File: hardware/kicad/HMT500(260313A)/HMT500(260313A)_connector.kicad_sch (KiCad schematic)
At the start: 10 parts, among them J1 SM08B-GHS-TB, J5 CHASSIS wire

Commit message: Schematic v0.9 + placement rev 4: apply triple-review A/B items, re-review fixes
- Power: OVP 32.6 V (R5 36.5k), D2 TVS3301, C2 2.2u 100V, buck input 220n x2,
  U2 pin 3 = SW; TPS26611 +Vs emitter-follower clamp (Q1 MMBTA06, R50, D50 27V)
- RS-485: THVD2410, DE 10k pull-down (R60) for in-house bootloader
- MCU: SGOOD on PA0/PA4, CS_CDC PA15, VIN_SENSE PB0, LATCH/CS pull-ups,
  SWD no-connect removed, netlist checker flags no-connect on used pins
- Analog: OPA197 V+ = DAC AVDD, R31/R41 100k, local caps; X7R throughout
- New aux sheet; SOT-23 and R1206 footprints; parts list and JLC files
- Placement: pin-targeted hints, MCU decaps under U4, chassis parts grouped
  in front, J5 keep-out 3.3 mm, CHASSIS netclass; 102/102 parts placed
- Docs: final review H table, decision #32, circuit design, placement rev 4

Co-Authored-By: Claude Opus 5.5 <noreply@anthropic.com>
Claude-Session: https://claude.ai/code/session_01JA2o8uJsqp9Vzsg4b665ev
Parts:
- D2: value SMBJ33CA -> TVS3301DRBR; footprint Diode_SMD:D_SMB -> HMT500_260313A:Texas_DRB0008A_PadFloat; symbol HMT500_260313A:TVS_BI -> HMT500_260313A:TVS3301
- R2: value 1M -> 1M HV; footprint Resistor_SMD:R_0603_1608Metric -> Resistor_SMD:R_1206_3216Metric
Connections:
- net GND: now also D2.5, D2.6, D2.7, D2.8; no longer D2.2
- net VIN_F: now also D2.2, D2.3, D2.4
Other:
- note added: "4.7n Y2 / 1M HV"
- note added: "SMDJ 3 kW (1st) -> R1 -> TVS3301 flat clamp (2nd) -> eFuse on sheet Power"
- note added: "TI 평탄 클램프 ±33 V, 42.5 V @ 27 A — 음(-) 서지에서 eFuse IN–OUT을 -70 V/10 ms 이내로 (전원 ≤ 28 V, 여유 작음 → 몰딩 전 서지 시험). DC 입력 33 V 초과 금지 (v0.9, 이전 SMBJ33CA)"
- note added: "TVS3301DRBR"
- note added: "Y2 안전 콘덴서 + 1 MΩ 고전압 칩 저항 1206 (사용 전압 ≥ 1 kV — GDT 방전 전 임펄스를 견딤, 몰딩 안)"
- note removed: "4.7n Y2 / 1M"
- note removed: "SMBJ33CA"
- note removed: "SMDJ 3 kW (1st) -> R1 -> SMBJ (2nd) -> eFuse on sheet Power"
- note removed: "TVS 양방향 600 W, 33 V — eFuse 정격 이하로 제한"
- note removed: "Y2 안전 콘덴서 + 1 MΩ 정전기 방전 경로"

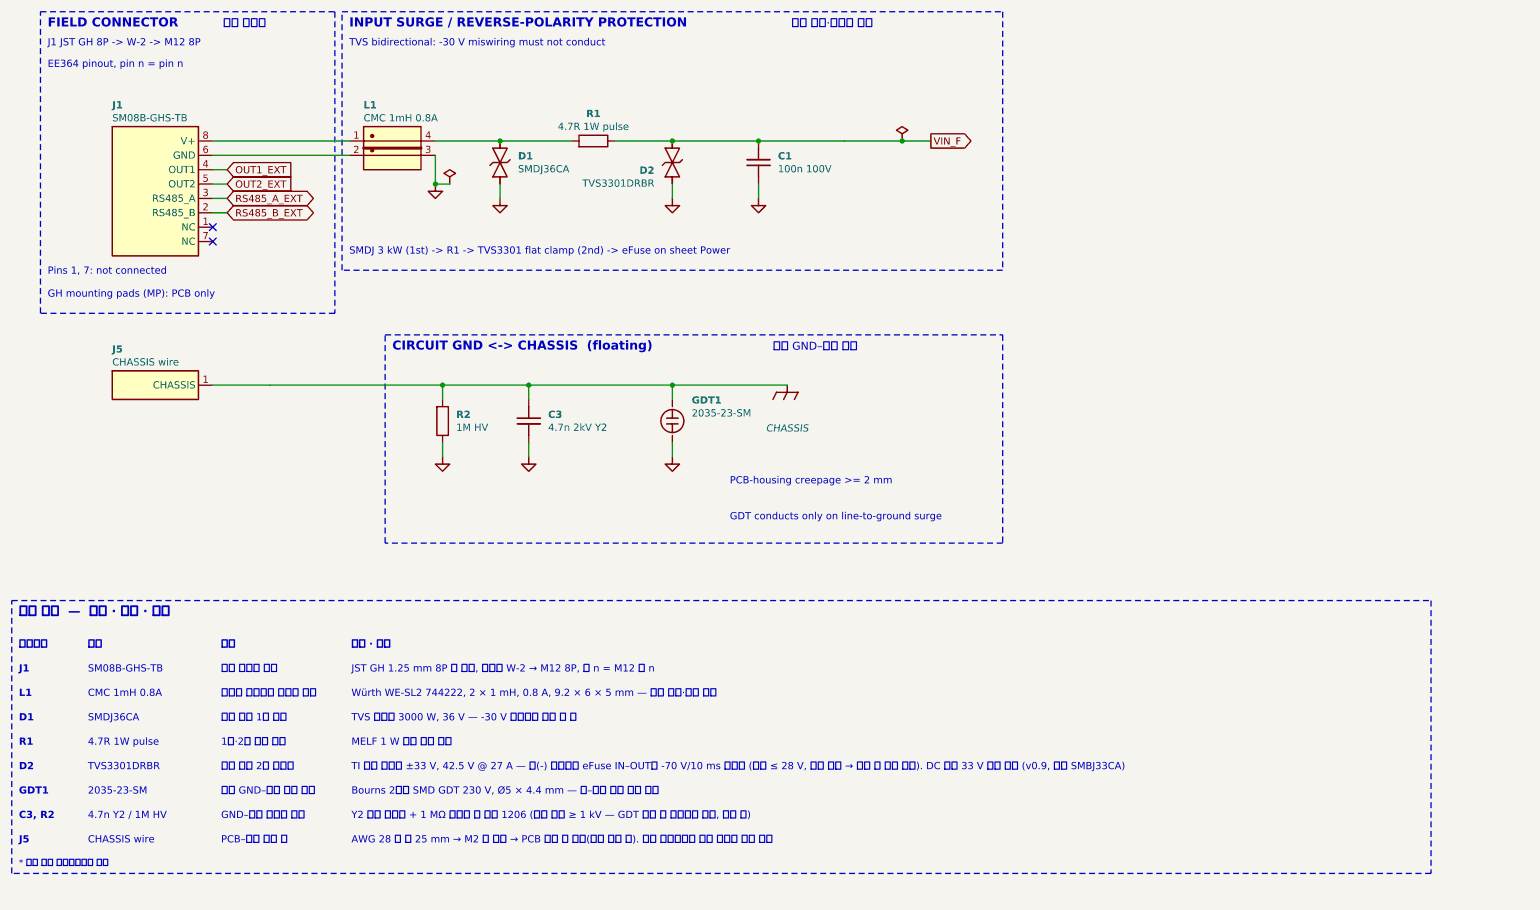
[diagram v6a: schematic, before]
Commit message: Map BOM to JLCPCB/LCSC parts (decision #34) and re-place
- 50 of 55 BOM lines have LCSC numbers (make_parts_list.LCSC); parts list
  gets LCSC / JLC class columns; JLC BOM and harness order filled
- Keep MCU (125 C grade), LMR36006, R19 precision ref and pulse resistors
  via JLC global sourcing
- LCSC-driven footprint changes: C6/C10 1210, C16/C17 0805, R1 2512,
  L2 XAL4040; C3 2 kV X7R 1812, GDT 2035-25, L1 SRF0905 (to verify)
- Re-placed: 102/102, netlist 77/77, assembly sim 23 OK

Co-Authored-By: Claude Opus 5.5 <noreply@anthropic.com>
Claude-Session: https://claude.ai/code/session_01JA2o8uJsqp9Vzsg4b665ev
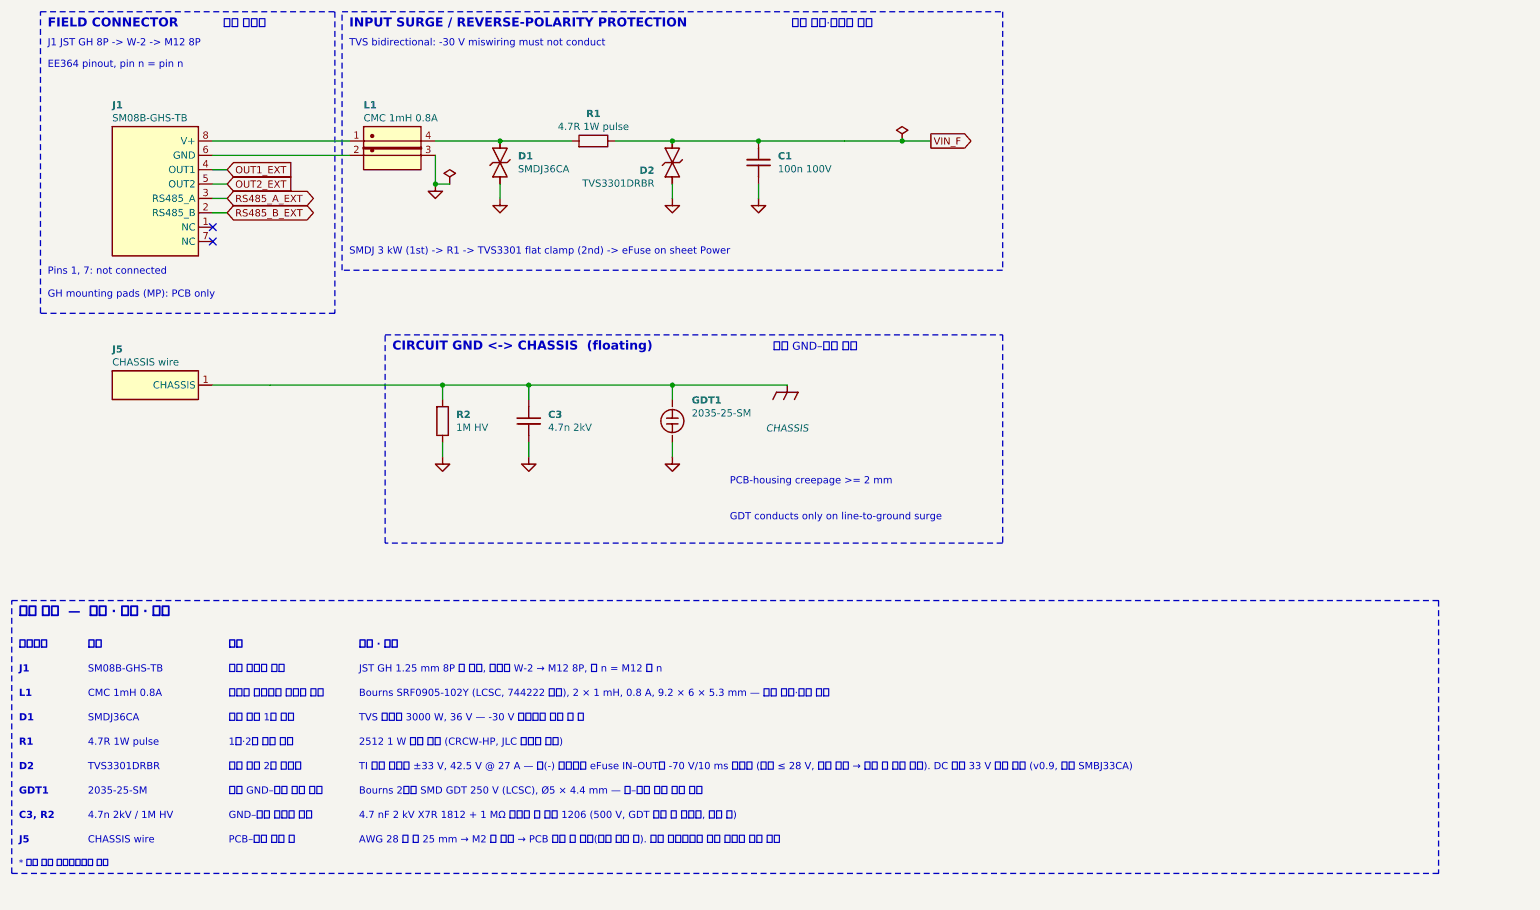
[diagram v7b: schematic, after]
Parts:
- C3: value 4.7n 2kV Y2 -> 4.7n 2kV
- GDT1: value 2035-23-SM -> 2035-25-SM
- R1: footprint Resistor_SMD:R_MELF_MMB-0207 -> Resistor_SMD:R_2512_6332Metric
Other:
- note added: "2035-25-SM"
- note added: "2512 1 W 펄스 내성 (CRCW-HP, JLC 글로벌 소싱)"
- note added: "4.7 nF 2 kV X7R 1812 + 1 MΩ 서지용 칩 저항 1206 (500 V, GDT 방전 전 임펄스, 몰딩 안)"
- note added: "4.7n 2kV / 1M HV"
- note added: "Bourns 2전극 SMD GDT 250 V (LCSC), Ø5 × 4.4 mm — 선–대지 서지 때만 도통"
- note added: "Bourns SRF0905-102Y (LCSC, 744222 동등), 2 × 1 mH, 0.8 A, 9.2 × 6 × 5.3 mm — 전도 방출·내성 대책"
- note removed: "2035-23-SM"
- note removed: "4.7n Y2 / 1M HV"
- note removed: "Bourns 2전극 SMD GDT 230 V, Ø5 × 4.4 mm — 선–대지 서지 때만 도통"
- note removed: "MELF 1 W 펄스 내량 저항"
- note removed: "Würth WE-SL2 744222, 2 × 1 mH, 0.8 A, 9.2 × 6 × 5 mm — 전도 방출·내성 대책"
- note removed: "Y2 안전 콘덴서 + 1 MΩ 고전압 칩 저항 1206 (사용 전압 ≥ 1 kV — GDT 방전 전 임펄스를 견딤, 몰딩 안)"

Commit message: Apply agreed external review items (decision #35)
- H01: series 100 V Schottky D3 (PMEG10010ELR) between D2 and eFuse IN
  (new net VIN_D) so negative surges no longer stress U1 IN-OUT
- H02: RS-485 bus TVS D60/D61 (TVS3301); U11 -> THVD2410DGKR (VSSOP-8)
- H04: +Vs clamp zener 27 V -> 24 V (BZX84C24LT1G)
- H08: ADS1220 IDAC fixed at 250 uA
- Room for new parts: C7 removed, 37 low-voltage R/C moved to 0402
  (LCSC basic where available); chassis parts keep CH_GAP between each other
- Placement 104/104, netlist 78/78, pcbnew DRC: no clearance errors,
  assembly sim 23 OK; parts list / JLC BOM updated
- docs/hw/external-review-response-260930.md: item responses, output load
  table, current budget, firmware requirements F1-F6, tests T1-T7

Co-Authored-By: Claude Opus 5.5 <noreply@anthropic.com>
Claude-Session: https://claude.ai/code/session_01JA2o8uJsqp9Vzsg4b665ev
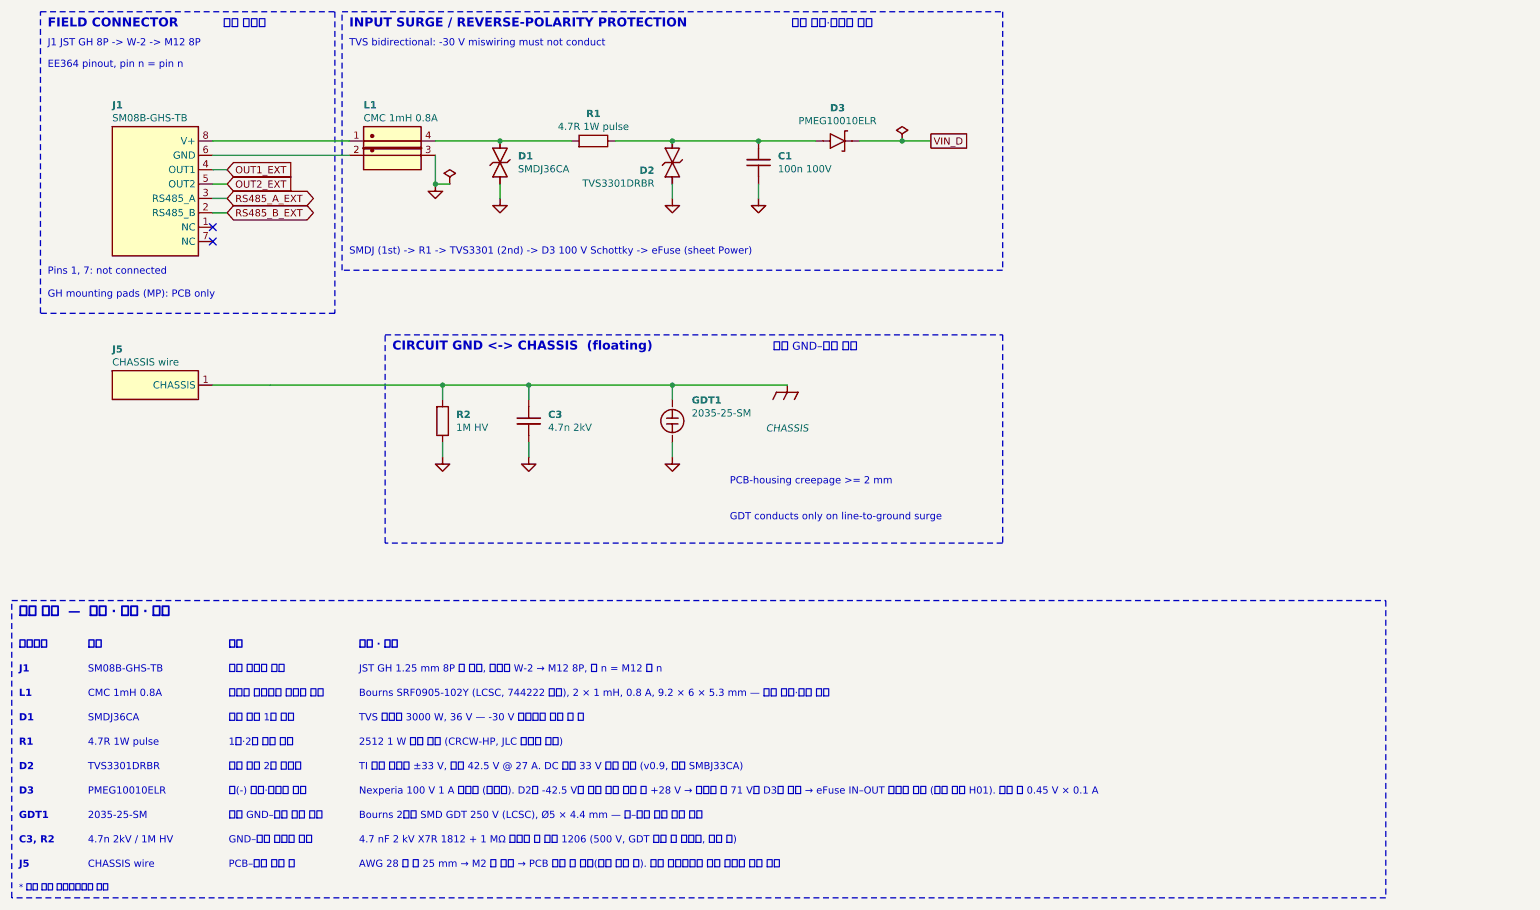
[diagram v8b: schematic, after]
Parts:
- added D3: PMEG10010ELR, Diode_SMD:D_SOD-123F, symbol HMT500_260313A:SCHOTTKY
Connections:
- net VIN_F: no longer names the net of C1.1, D2.1, D2.2, D2.3, D2.4, R1.2
- net VIN_F: now also D3.2
- new net VIN_D: D3.1
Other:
- note added: "D3"
- note added: "Nexperia 100 V 1 A 쇼트키 (저누설). D2가 -42.5 V로 잡는 동안 출력 쪽 +28 V → 역전압 약 71 V를 D3가 받음 → eFuse IN–OUT 역전압 없음 (외부 검수 H01). 손실 약 0.45 V × 0.1 A"
- note added: "PMEG10010ELR"
- note added: "SMDJ (1st) -> R1 -> TVS3301 (2nd) -> D3 100 V Schottky -> eFuse (sheet Power)"
- note added: "TI 평탄 클램프 ±33 V, 최대 42.5 V @ 27 A. DC 입력 33 V 초과 금지 (v0.9, 이전 SMBJ33CA)"
- note added: "음(-) 서지·역극성 차단"
- note removed: "SMDJ 3 kW (1st) -> R1 -> TVS3301 flat clamp (2nd) -> eFuse on sheet Power"
- note removed: "TI 평탄 클램프 ±33 V, 42.5 V @ 27 A — 음(-) 서지에서 eFuse IN–OUT을 -70 V/10 ms 이내로 (전원 ≤ 28 V, 여유 작음 → 몰딩 전 서지 시험). DC 입력 33 V 초과 금지 (v0.9, 이전 SMBJ33CA)"
